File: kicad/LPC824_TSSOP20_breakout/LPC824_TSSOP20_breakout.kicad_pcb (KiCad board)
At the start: 2 copper layers, 4 parts, among them J1 PINS_1X10, J2 PINS_1X10, M1 LPC824M201JDH20

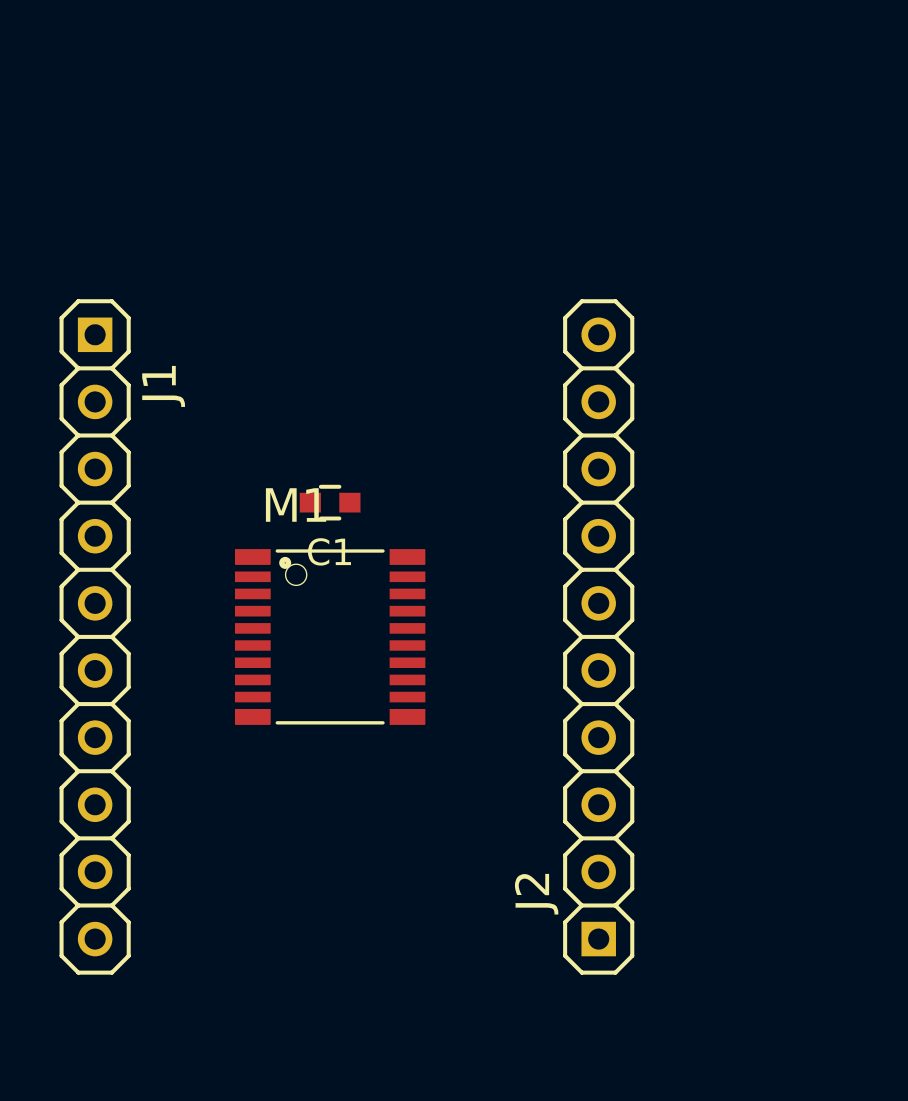
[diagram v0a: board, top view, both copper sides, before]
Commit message: * completed breakout board schematic * started with layout of breakout
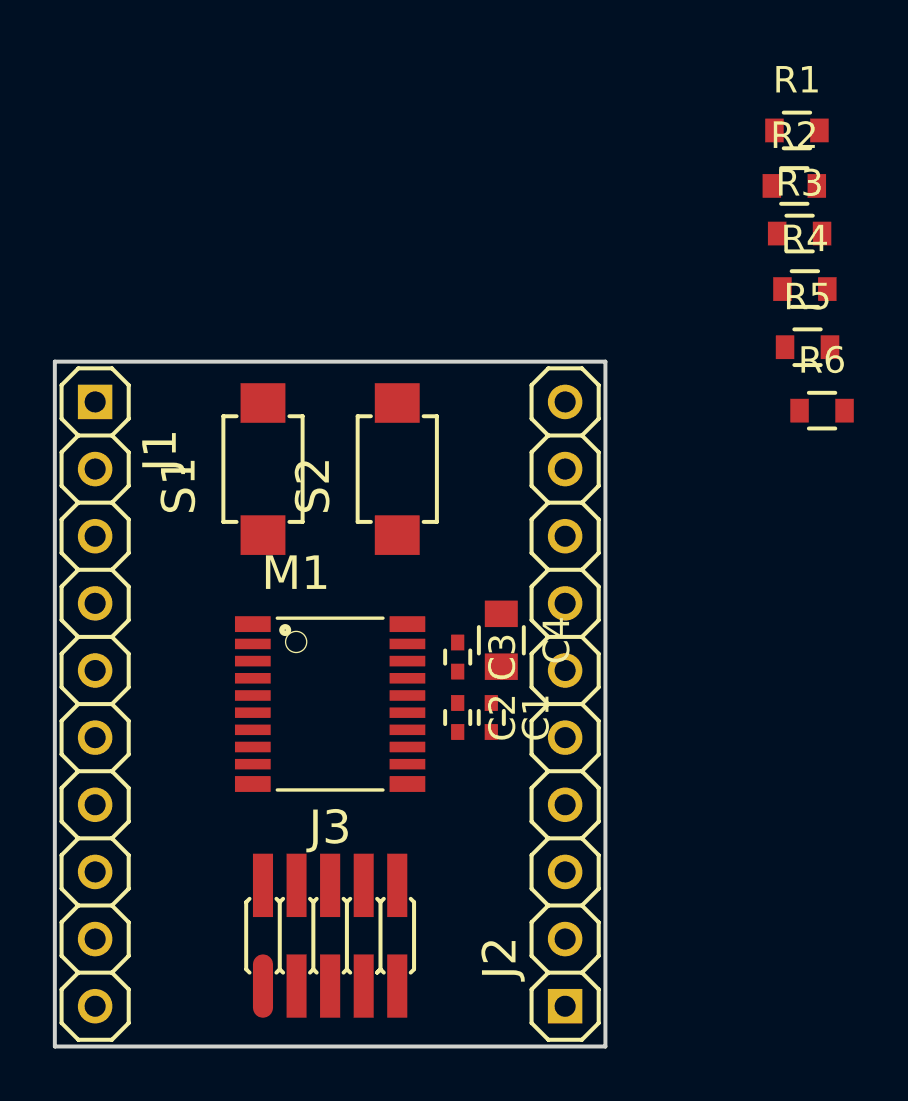
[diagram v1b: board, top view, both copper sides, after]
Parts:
- added C2: 10n, SquantorRcl:C_0402, F.Cu at (153.4, 102.1)
- added C3: 100n, SquantorRcl:C_0402, F.Cu at (153.4, 99.8)
- added C4: 10u, SquantorRcl:C_0805, F.Cu at (155.1, 99.2)
- added J3: JTAG_2X05, SquantorConnectors:Header-0127-2X05-SMD, F.Cu at (148.6, 110.4)
- added R1: 0, SquantorRcl:R_0603_hand, F.Cu at (166.2, 79.9)
- added R2: 0, SquantorRcl:R_0603_hand, F.Cu at (166.2, 82.0)
- added R3: 100k, SquantorRcl:R_0603_hand, F.Cu at (166.3, 83.8)
- added R4: 10k, SquantorRcl:R_0603_hand, F.Cu at (166.6, 85.9)
- added R5: 10K, SquantorRcl:R_0603_hand, F.Cu at (166.7, 88.1)
- added R6: 10K, SquantorRcl:R_0603_hand, F.Cu at (167.2, 90.5)
- added S1: 2pin_tact_switch, SquantorButtons:TD-85XU, F.Cu at (146.1, 92.7)
- added S2: 2pin_tact_switch, SquantorButtons:TD-85XU, F.Cu at (151.1, 92.7)
- C1: value C -> 100n; footprint SquantorRcl:C_0603 -> SquantorRcl:C_0402
- moved C1 10.2 mm to (154.7, 102.1), turned to 270 degrees
- moved J2 2.84 mm to (157.5, 101.6)
- moved J1 2.54 mm to (139.7, 101.6)
- moved M1 2.54 mm to (148.6, 101.6)
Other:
- board outline added: 20.8 x 25.9 mm
